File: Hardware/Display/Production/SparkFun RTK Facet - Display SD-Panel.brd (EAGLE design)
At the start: 118.6 x 193.8 mm, 662 parts, among them J1 FPC_12_0.5MM_BACKFLIP, J10 FPC_12_0.5MM_BACKFLIP, J11 FPC_12_0.5MM_BACKFLIP, J12 MICRO-SD-PUSH-PUSH-EXT-PIN, J13 FPC_12_0.5MM_BACKFLIP, J14 FPC_12_0.5MM_BACKFLIP, J15 MICRO-SD-PUSH-PUSH-EXT-PIN, J16 FPC_12_0.5MM_BACKFLIP, J17 FPC_12_0.5MM_BACKFLIP, J18 MICRO-SD-PUSH-PUSH-EXT-PIN, J19 FPC_12_0.5MM_BACKFLIP, J2 MICRO-SD-PUSH-PUSH-EXT-PIN, J20 FPC_12_0.5MM_BACKFLIP, J21 MICRO-SD-PUSH-PUSH-EXT-PIN, J22 FPC_12_0.5MM_BACKFLIP, J23 FPC_12_0.5MM_BACKFLIP, J24 MICRO-SD-PUSH-PUSH-EXT-PIN, J25 FPC_12_0.5MM_BACKFLIP, J26 FPC_12_0.5MM_BACKFLIP, J27 MICRO-SD-PUSH-PUSH-EXT-PIN, J28 FPC_12_0.5MM_BACKFLIP, J29 FPC_12_0.5MM_BACKFLIP, J3 FPC_12_0.5MM_BACKFLIP, J30 MICRO-SD-PUSH-PUSH-EXT-PIN, J31 FPC_12_0.5MM_BACKFLIP, J32 FPC_12_0.5MM_BACKFLIP, J33 MICRO-SD-PUSH-PUSH-EXT-PIN, J34 FPC_12_0.5MM_BACKFLIP, J35 FPC_12_0.5MM_BACKFLIP, J36 MICRO-SD-PUSH-PUSH-EXT-PIN, J37 FPC_12_0.5MM_BACKFLIP, J38 FPC_12_0.5MM_BACKFLIP, J39 MICRO-SD-PUSH-PUSH-EXT-PIN, J4 FPC_12_0.5MM_BACKFLIP, J40 FPC_12_0.5MM_BACKFLIP, J41 FPC_12_0.5MM_BACKFLIP, J42 MICRO-SD-PUSH-PUSH-EXT-PIN, J43 FPC_12_0.5MM_BACKFLIP, J44 FPC_12_0.5MM_BACKFLIP, J45 MICRO-SD-PUSH-PUSH-EXT-PIN, J46 FPC_12_0.5MM_BACKFLIP, J47 FPC_12_0.5MM_BACKFLIP, J48 MICRO-SD-PUSH-PUSH-EXT-PIN, J5 FPC_12_0.5MM_BACKFLIP, J6 MICRO-SD-PUSH-PUSH-EXT-PIN, J7 FPC_12_0.5MM_BACKFLIP, J8 FPC_12_0.5MM_BACKFLIP, J9 MICRO-SD-PUSH-PUSH-EXT-PIN, U1 LIS2DH12, U10 LIS2DH12, U11 LIS2DH12, U12 LIS2DH12, U13 LIS2DH12, U14 LIS2DH12, U15 LIS2DH12, U16 LIS2DH12, U2 LIS2DH12, U3 LIS2DH12, U4 LIS2DH12, U5 LIS2DH12, U6 LIS2DH12, U7 LIS2DH12, U8 LIS2DH12, U9 LIS2DH12

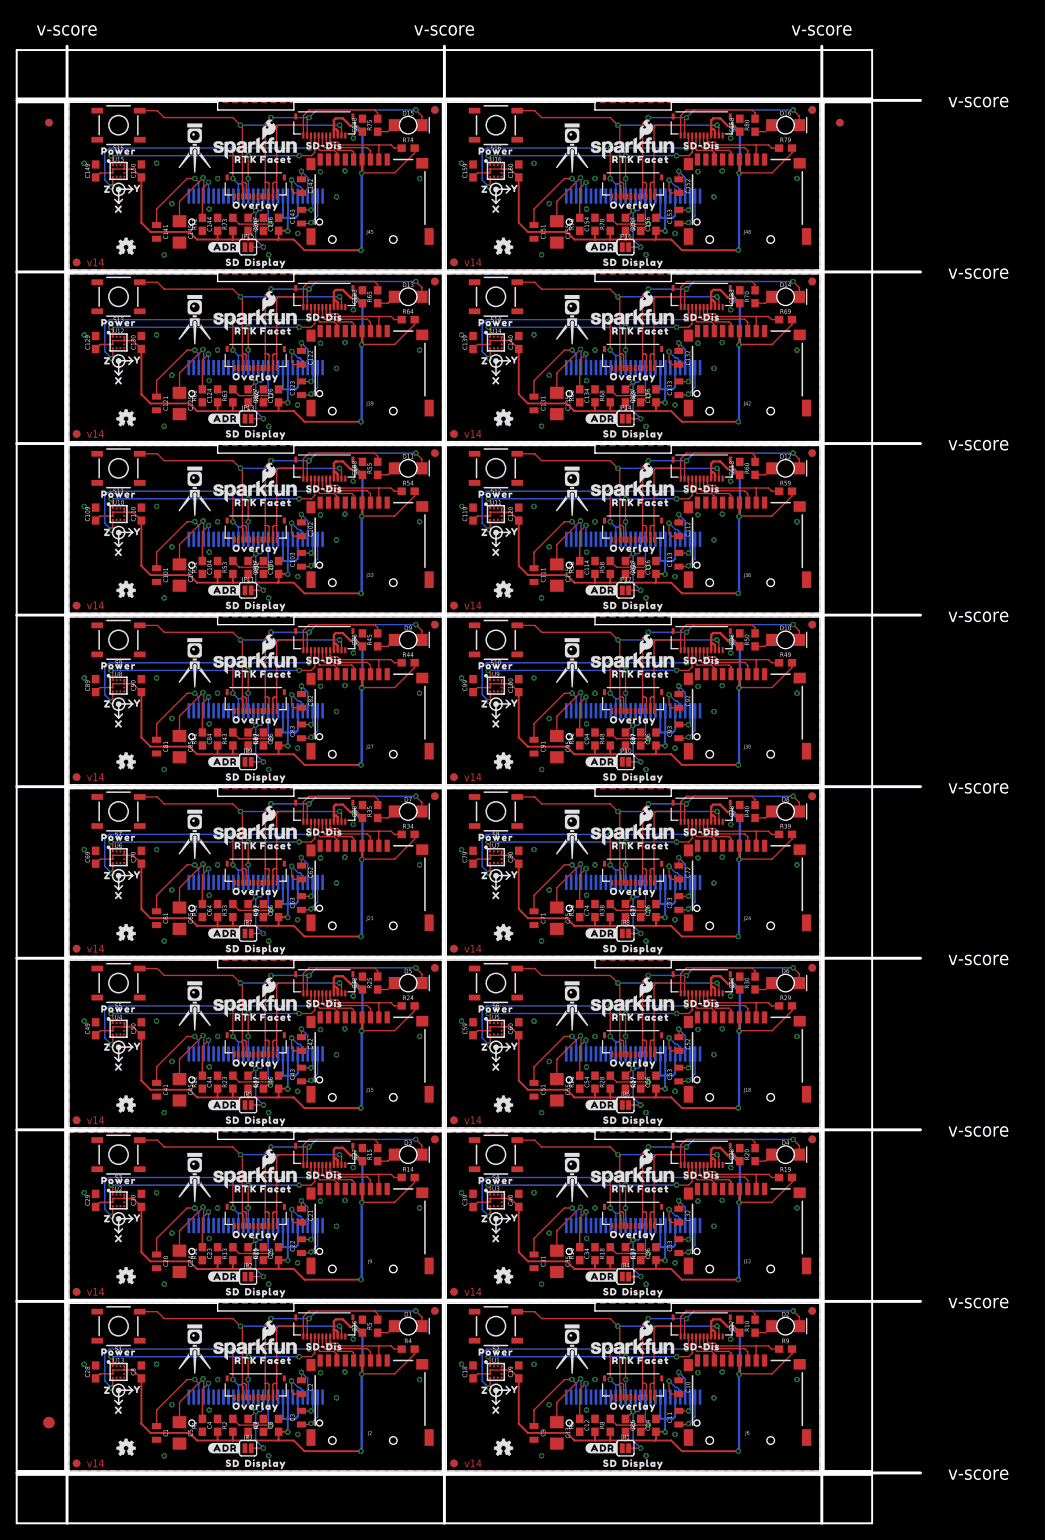
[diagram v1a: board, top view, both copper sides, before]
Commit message: Change to LIF 6 pin connector, remove GND plane around accel.
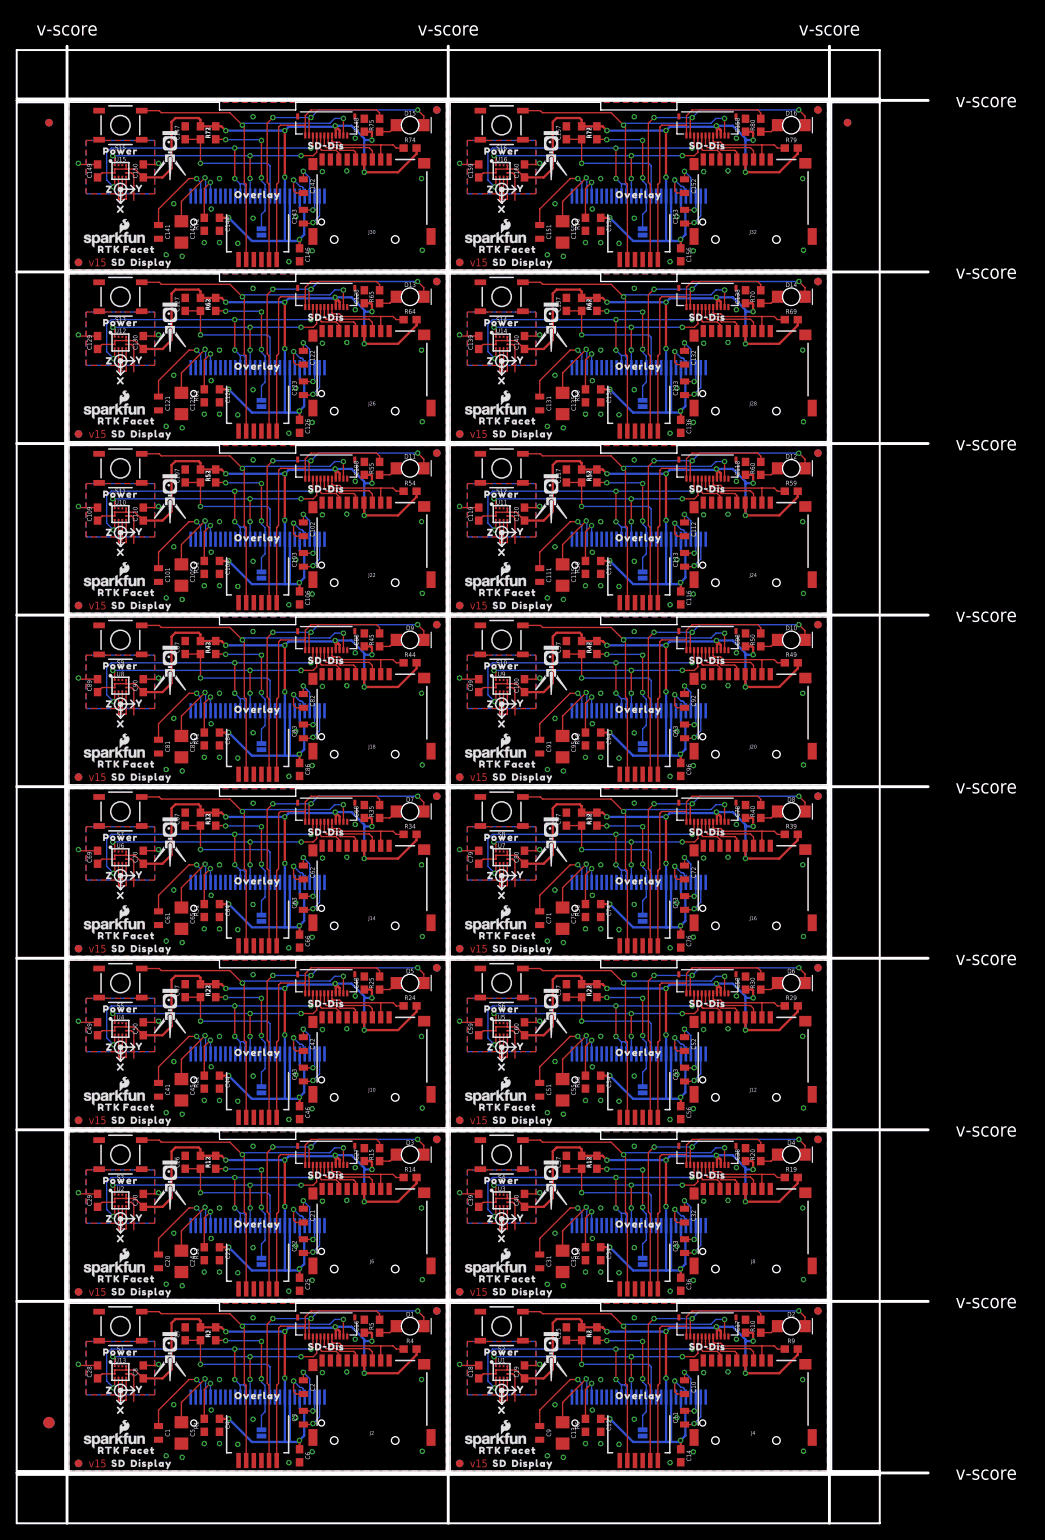
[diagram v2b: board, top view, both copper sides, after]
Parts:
- removed J33, J36, J39, J42, J45, J48: MICRO-SD-PUSH-PUSH-EXT-PIN, SparkFun-Connectors:MICROSD-EXTERNALPIN
- removed J34, J35, J37, J38, J40, J41, J43, J44, J46, J47: FPC_12_0.5MM_BACKFLIP, RTK Facet:FPC_12_DOUBLESIDED_BACKFLIP
- added JP17, JP19, JP21, JP23, JP25, JP27, JP29, JP31: (no value), SparkFun-Jumpers:SMT-JUMPER_2_NO_SILK
- added JP18, JP20, JP22, JP24, JP26, JP28, JP30, JP32: CONN_06, 1mm Pitch Connector:FPC_6_1MM-LIF
- J10, J14, J16, J20, J22, J26, J28, J32, J4, J8: value FPC_12_0.5MM_BACKFLIP -> MICRO-SD-PUSH-PUSH-EXT-PIN; device RTK Facet:FPC_12_DOUBLESIDED_BACKFLIP -> SparkFun-Connectors:MICROSD-EXTERNALPIN
- J15, J21, J27, J9: value MICRO-SD-PUSH-PUSH-EXT-PIN -> FPC_12_0.5MM_BACKFLIP; device SparkFun-Connectors:MICROSD-EXTERNALPIN -> RTK Facet:FPC_12_DOUBLESIDED_BACKFLIP
- JP1, JP10, JP12, JP14, JP16, JP4, JP6, JP8: value (none) -> CONN_06; device SparkFun-Jumpers:SMT-JUMPER_2_NO_SILK -> 1mm Pitch Connector:FPC_6_1MM-LIF
- LOGO10, LOGO12, LOGO14, LOGO16, LOGO18, LOGO2, LOGO20, LOGO22, LOGO24, LOGO26, LOGO28, LOGO30, LOGO32, LOGO5, LOGO6, LOGO8: value SFE_LOGO_NAME_FLAME.1_INCH -> SFE_LOGO_NAME_FLAME8_MM; device SparkFun-Aesthetics:SFE_LOGO_NAME_FLAME_.1 -> SparkFun-Aesthetics:SFE_LOGO_NAME_FLAME_8MM
- moved JP15 102.1 mm to (75.3, 72.5), flipped to the bottom, turned to 90 degrees
- moved JP16 88.7 mm to (74.8, 71.9), turned to 180 degrees
- moved J29 85.6 mm to (33.8, 176.6)
- moved J30 83.6 mm to (39.8, 161.6)
- moved JP11 83.5 mm to (75.3, 50.0), flipped to the bottom, turned to 90 degrees
- moved JP14 81.9 mm to (24.8, 71.9), turned to 180 degrees
- moved J32 75.5 mm to (89.8, 161.6), turned to 0 degrees
- moved J27 74.6 mm to (83.8, 154.0), turned to 180 degrees
- moved J31 67.5 mm to (83.8, 176.6)
- moved JP7 67.3 mm to (75.3, 27.5), flipped to the bottom, turned to 90 degrees
- moved J20 67.1 mm to (89.8, 94.0), turned to 0 degrees
- moved J18 66.7 mm to (39.8, 94.0)
- moved J17 66.6 mm to (33.8, 109.0)
- moved JP12 66.2 mm to (74.8, 49.4), turned to 180 degrees
- moved J8 65.6 mm to (89.8, 26.5), turned to 0 degrees
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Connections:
- net 3.3V1: now also J3.3, J3.4; no longer J4.3, J6.4
- net 3.3V10: now also J21.3, J21.4, J22.4; no longer J31.3, J31.4, J33.4
- net 3.3V11: now also J23.3, J23.4, J24.4; no longer J34.3, J34.4, J36.4
- net 3.3V12: now also J25.3, J25.4, J26.4; no longer J37.3, J37.4, J39.4
- net 3.3V13: now also J27.3, J27.4, J28.4; no longer J40.3, J40.4, J42.4
- net 3.3V14: now also J29.3, J29.4, J30.4; no longer J43.3, J43.4, J45.4
- net 3.3V15: now also J31.3, J31.4, J32.4; no longer J46.3, J46.4, J48.4
- net 3.3V2: now also J5.3, J5.4, J6.4; no longer J7.3, J7.4, J9.4
- net 3.3V3: now also J7.3, J7.4, J8.4; no longer J10.3, J10.4, J12.4
- net 3.3V4: now also J10.4, J9.3, J9.4; no longer J13.3, J13.4, J15.4
- net 3.3V5: now also J11.3, J11.4, J12.4; no longer J16.3, J16.4, J18.4
- net 3.3V6: now also J13.3, J13.4, J14.4; no longer J19.3, J19.4, J21.4
- net 3.3V7: now also J15.3, J15.4, J16.4; no longer J22.3, J22.4, J24.4
- net 3.3V8: now also J17.3, J17.4, J18.4; no longer J25.3, J25.4, J27.4
- net 3.3V9: now also J19.3, J19.4, J20.4; no longer J28.3, J28.4, J30.4
- net CHARGE_LED: now also JP1.2; no longer J3.3, J3.4
- net CHARGE_LED1: now also J3.11, JP4.2; no longer J4.11, J5.3, J5.4
- net CHARGE_LED10: now also J21.11, JP22.2; no longer J31.11, J32.3, J32.4
- net CHARGE_LED11: now also J23.11, JP24.2; no longer J34.11, J35.3, J35.4
- net CHARGE_LED12: now also J25.11, JP26.2; no longer J37.11, J38.3, J38.4
- net CHARGE_LED13: now also J27.11, JP28.2; no longer J40.11, J41.3, J41.4
- net CHARGE_LED14: now also J29.11, JP30.2; no longer J43.11, J44.3, J44.4
- net CHARGE_LED15: now also J31.11, JP32.2; no longer J46.11, J47.3, J47.4
- net CHARGE_LED2: now also J5.11, JP6.2; no longer J7.11, J8.3, J8.4
- net CHARGE_LED3: now also J7.11, JP8.2; no longer J10.11, J11.3, J11.4
- net CHARGE_LED4: now also J9.11, JP10.2; no longer J13.11, J14.3, J14.4
- net CHARGE_LED5: now also J11.11, JP12.2; no longer J16.11, J17.3, J17.4
- net CHARGE_LED6: now also J13.11, JP14.2; no longer J19.11, J20.3, J20.4
- net CHARGE_LED7: now also J15.11, JP16.2; no longer J22.11, J23.3, J23.4
- net CHARGE_LED8: now also J17.11, JP18.2; no longer J25.11, J26.3, J26.4
- net CHARGE_LED9: now also J19.11, JP20.2; no longer J28.11, J29.3, J29.4
- net D/C1: now also JP2.2; no longer JP1.2
- net D/C10: now also JP21.2; no longer JP11.2
- net D/C11: now also JP23.2; no longer JP12.2
- net D/C12: now also JP25.2; no longer JP13.2
- net D/C13: now also JP27.2; no longer JP14.2
- net D/C14: now also JP29.2; no longer JP15.2
- net D/C15: now also JP31.2; no longer JP16.2
- net D/C2: now also JP5.2; no longer JP2.2
- net D/C3: now also JP7.2; no longer JP4.2
- net D/C4: now also JP9.2; no longer JP5.2
- net D/C5: now also JP11.2; no longer JP6.2
- net D/C6: now also JP13.2; no longer JP7.2
- net D/C7: now also JP15.2; no longer JP8.2
- net D/C8: now also JP17.2; no longer JP9.2
- net D/C9: now also JP19.2; no longer JP10.2
- net ESP_21/SDA1: now also J3.10; no longer J4.10
- net ESP_21/SDA10: now also J21.10; no longer J31.10
- net ESP_21/SDA11: now also J23.10; no longer J34.10
- net ESP_21/SDA12: now also J25.10; no longer J37.10
- net ESP_21/SDA13: now also J27.10; no longer J40.10
- net ESP_21/SDA14: now also J29.10; no longer J43.10
- net ESP_21/SDA15: now also J31.10; no longer J46.10
- net ESP_21/SDA2: now also J5.10; no longer J7.10
- net ESP_21/SDA3: now also J7.10; no longer J10.10
- net ESP_21/SDA4: now also J9.10; no longer J13.10
- net ESP_21/SDA5: now also J11.10; no longer J16.10
- net ESP_21/SDA6: now also J13.10; no longer J19.10
- net ESP_21/SDA7: now also J15.10; no longer J22.10
- net ESP_21/SDA8: now also J17.10; no longer J25.10
- net ESP_21/SDA9: now also J19.10; no longer J28.10
- net ESP_22/SCL1: now also J3.9; no longer J4.9
- net ESP_22/SCL10: now also J21.9; no longer J31.9
- net ESP_22/SCL11: now also J23.9; no longer J34.9
- net ESP_22/SCL12: now also J25.9; no longer J37.9
- net ESP_22/SCL13: now also J27.9; no longer J40.9
- net ESP_22/SCL14: now also J29.9; no longer J43.9
- net ESP_22/SCL15: now also J31.9; no longer J46.9
- net ESP_22/SCL2: now also J5.9; no longer J7.9
- net ESP_22/SCL3: now also J7.9; no longer J10.9
- net ESP_22/SCL4: now also J9.9; no longer J13.9
- net ESP_22/SCL5: now also J11.9; no longer J16.9
- net ESP_22/SCL6: now also J13.9; no longer J19.9
- net ESP_22/SCL7: now also J15.9; no longer J22.9
- net ESP_22/SCL8: now also J17.9; no longer J25.9
- net ESP_22/SCL9: now also J19.9; no longer J28.9
- net GND: now also JP1.6; no longer J3.11, J3.12
- net GND1: now also J3.1, J4.10, J4.11, J4.12, J4.13, J4.6, J4.9, JP2.1, JP4.6; no longer J4.1, J5.11, J5.12, J6.10, J6.11, J6.12, J6.13, J6.6, J6.9, JP1.1
- net GND10: now also J21.1, J22.10, J22.11, J22.12, J22.13, J22.6, J22.9, JP21.1, JP22.6; no longer J31.1, J32.11, J32.12, J33.10, J33.11, J33.12, J33.13, J33.6, J33.9, JP11.1
- net GND11: now also J23.1, J24.10, J24.11, J24.12, J24.13, J24.6, J24.9, JP23.1, JP24.6; no longer J34.1, J35.11, J35.12, J36.10, J36.11, J36.12, J36.13, J36.6, J36.9, JP12.1
- net GND12: now also J25.1, J26.10, J26.11, J26.12, J26.13, J26.6, J26.9, JP25.1, JP26.6; no longer J37.1, J38.11, J38.12, J39.10, J39.11, J39.12, J39.13, J39.6, J39.9, JP13.1
- net GND13: now also J27.1, J28.10, J28.11, J28.12, J28.13, J28.6, J28.9, JP27.1, JP28.6; no longer J40.1, J41.11, J41.12, J42.10, J42.11, J42.12, J42.13, J42.6, J42.9, JP14.1
- net GND14: now also J29.1, J30.10, J30.11, J30.12, J30.13, J30.6, J30.9, JP29.1, JP30.6; no longer J43.1, J44.11, J44.12, J45.10, J45.11, J45.12, J45.13, J45.6, J45.9, JP15.1
- net GND15: now also J31.1, J32.10, J32.11, J32.12, J32.13, J32.6, J32.9, JP31.1, JP32.6; no longer J46.1, J47.11, J47.12, J48.10, J48.11, J48.12, J48.13, J48.6, J48.9, JP16.1
- net GND2: now also J5.1, J6.10, J6.11, J6.12, J6.13, J6.6, J6.9, JP5.1, JP6.6; no longer J7.1, J8.11, J8.12, J9.10, J9.11, J9.12, J9.13, J9.6, J9.9, JP2.1
- net GND3: now also J7.1, J8.10, J8.11, J8.12, J8.13, J8.6, J8.9, JP7.1, JP8.6; no longer J10.1, J11.11, J11.12, J12.10, J12.11, J12.12, J12.13, J12.6, J12.9, JP4.1
- net GND4: now also J10.10, J10.11, J10.12, J10.13, J10.6, J10.9, J9.1, JP10.6, JP9.1; no longer J13.1, J14.11, J14.12, J15.10, J15.11, J15.12, J15.13, J15.6, J15.9, JP5.1
- net GND5: now also J11.1, J12.10, J12.11, J12.12, J12.13, J12.6, J12.9, JP11.1, JP12.6; no longer J16.1, J17.11, J17.12, J18.10, J18.11, J18.12, J18.13, J18.6, J18.9, JP6.1
- net GND6: now also J13.1, J14.10, J14.11, J14.12, J14.13, J14.6, J14.9, JP13.1, JP14.6; no longer J19.1, J20.11, J20.12, J21.10, J21.11, J21.12, J21.13, J21.6, J21.9, JP7.1
- net GND7: now also J15.1, J16.10, J16.11, J16.12, J16.13, J16.6, J16.9, JP15.1, JP16.6; no longer J22.1, J23.11, J23.12, J24.10, J24.11, J24.12, J24.13, J24.6, J24.9, JP8.1
- net GND8: now also J17.1, J18.10, J18.11, J18.12, J18.13, J18.6, J18.9, JP17.1, JP18.6; no longer J25.1, J26.11, J26.12, J27.10, J27.11, J27.12, J27.13, J27.6, J27.9, JP9.1
- net GND9: now also J19.1, J20.10, J20.11, J20.12, J20.13, J20.6, J20.9, JP19.1, JP20.6; no longer J28.1, J29.11, J29.12, J30.10, J30.11, J30.12, J30.13, J30.6, J30.9, JP10.1
- net POWER_BTN: now also JP1.5; no longer J3.10, J3.9
- net POWER_BTN1: now also J3.2, JP4.5; no longer J4.2, J5.10, J5.9
- net POWER_BTN10: now also J21.2, JP22.5; no longer J31.2, J32.10, J32.9
- net POWER_BTN11: now also J23.2, JP24.5; no longer J34.2, J35.10, J35.9
- net POWER_BTN12: now also J25.2, JP26.5; no longer J37.2, J38.10, J38.9
- net POWER_BTN13: now also J27.2, JP28.5; no longer J40.2, J41.10, J41.9
- net POWER_BTN14: now also J29.2, JP30.5; no longer J43.2, J44.10, J44.9
- net POWER_BTN15: now also J31.2, JP32.5; no longer J46.2, J47.10, J47.9
- net POWER_BTN2: now also J5.2, JP6.5; no longer J7.2, J8.10, J8.9
- net POWER_BTN3: now also J7.2, JP8.5; no longer J10.2, J11.10, J11.9
- net POWER_BTN4: now also J9.2, JP10.5; no longer J13.2, J14.10, J14.9
- net POWER_BTN5: now also J11.2, JP12.5; no longer J16.2, J17.10, J17.9
- net POWER_BTN6: now also J13.2, JP14.5; no longer J19.2, J20.10, J20.9
- net POWER_BTN7: now also J15.2, JP16.5; no longer J22.2, J23.10, J23.9
- net POWER_BTN8: now also J17.2, JP18.5; no longer J25.2, J26.10, J26.9
- net POWER_BTN9: now also J19.2, JP20.5; no longer J28.2, J29.10, J29.9
- net SD_!CS!1: now also J3.5, J4.2; no longer J4.5, J6.2
- net SD_!CS!10: now also J21.5, J22.2; no longer J31.5, J33.2
- net SD_!CS!11: now also J23.5, J24.2; no longer J34.5, J36.2
- net SD_!CS!12: now also J25.5, J26.2; no longer J37.5, J39.2
- net SD_!CS!13: now also J27.5, J28.2; no longer J40.5, J42.2
- net SD_!CS!14: now also J29.5, J30.2; no longer J43.5, J45.2
- net SD_!CS!15: now also J31.5, J32.2; no longer J46.5, J48.2
- net SD_!CS!2: now also J5.5, J6.2; no longer J7.5, J9.2
- net SD_!CS!3: now also J7.5, J8.2; no longer J10.5, J12.2
- net SD_!CS!4: now also J10.2, J9.5; no longer J13.5, J15.2
- net SD_!CS!5: now also J11.5, J12.2; no longer J16.5, J18.2
- net SD_!CS!6: now also J13.5, J14.2; no longer J19.5, J21.2
- net SD_!CS!7: now also J15.5, J16.2; no longer J22.5, J24.2
- net SD_!CS!8: now also J17.5, J18.2; no longer J25.5, J27.2
- net SD_!CS!9: now also J19.5, J20.2; no longer J28.5, J30.2
- net SD_CIPO1: now also J3.8, J4.7; no longer J4.8, J6.7
- net SD_CIPO10: now also J21.8, J22.7; no longer J31.8, J33.7
- net SD_CIPO11: now also J23.8, J24.7; no longer J34.8, J36.7
- net SD_CIPO12: now also J25.8, J26.7; no longer J37.8, J39.7
- net SD_CIPO13: now also J27.8, J28.7; no longer J40.8, J42.7
- net SD_CIPO14: now also J29.8, J30.7; no longer J43.8, J45.7
- net SD_CIPO15: now also J31.8, J32.7; no longer J46.8, J48.7
- net SD_CIPO2: now also J5.8, J6.7; no longer J7.8, J9.7
- net SD_CIPO3: now also J7.8, J8.7; no longer J10.8, J12.7
- net SD_CIPO4: now also J10.7, J9.8; no longer J13.8, J15.7
- net SD_CIPO5: now also J11.8, J12.7; no longer J16.8, J18.7
- net SD_CIPO6: now also J13.8, J14.7; no longer J19.8, J21.7
- net SD_CIPO7: now also J15.8, J16.7; no longer J22.8, J24.7
- net SD_CIPO8: now also J17.8, J18.7; no longer J25.8, J27.7
- net SD_CIPO9: now also J19.8, J20.7; no longer J28.8, J30.7
- net SD_COPI1: now also J3.6, J4.3; no longer J4.6, J6.3
- net SD_COPI10: now also J21.6, J22.3; no longer J31.6, J33.3
- net SD_COPI11: now also J23.6, J24.3; no longer J34.6, J36.3
- net SD_COPI12: now also J25.6, J26.3; no longer J37.6, J39.3
- net SD_COPI13: now also J27.6, J28.3; no longer J40.6, J42.3
- net SD_COPI14: now also J29.6, J30.3; no longer J43.6, J45.3
- net SD_COPI15: now also J31.6, J32.3; no longer J46.6, J48.3
- net SD_COPI2: now also J5.6, J6.3; no longer J7.6, J9.3
- net SD_COPI3: now also J7.6, J8.3; no longer J10.6, J12.3
- net SD_COPI4: now also J10.3, J9.6; no longer J13.6, J15.3
- net SD_COPI5: now also J11.6, J12.3; no longer J16.6, J18.3
- net SD_COPI6: now also J13.6, J14.3; no longer J19.6, J21.3
- net SD_COPI7: now also J15.6, J16.3; no longer J22.6, J24.3
- net SD_COPI8: now also J17.6, J18.3; no longer J25.6, J27.3
- net SD_COPI9: now also J19.6, J20.3; no longer J28.6, J30.3
- net SD_SCK1: now also J3.7, J4.5; no longer J4.7, J6.5
- net SD_SCK10: now also J21.7, J22.5; no longer J31.7, J33.5
- net SD_SCK11: now also J23.7, J24.5; no longer J34.7, J36.5
- net SD_SCK12: now also J25.7, J26.5; no longer J37.7, J39.5
- net SD_SCK13: now also J27.7, J28.5; no longer J40.7, J42.5
- net SD_SCK14: now also J29.7, J30.5; no longer J43.7, J45.5
- net SD_SCK15: now also J31.7, J32.5; no longer J46.7, J48.5
- net SD_SCK2: now also J5.7, J6.5; no longer J7.7, J9.5
- net SD_SCK3: now also J7.7, J8.5; no longer J10.7, J12.5
- net SD_SCK4: now also J10.5, J9.7; no longer J13.7, J15.5
- net SD_SCK5: now also J11.7, J12.5; no longer J16.7, J18.5
- net SD_SCK6: now also J13.7, J14.5; no longer J19.7, J21.5
- net SD_SCK7: now also J15.7, J16.5; no longer J22.7, J24.5
- net SD_SCK8: now also J17.7, J18.5; no longer J25.7, J27.5
- net SD_SCK9: now also J19.7, J20.5; no longer J28.7, J30.5
- net V_USB: now also JP1.1; no longer J3.1, J3.2
- net V_USB1: now also J3.12, JP4.1; no longer J4.12, J5.1, J5.2
- net V_USB10: now also J21.12, JP22.1; no longer J31.12, J32.1, J32.2
- net V_USB11: now also J23.12, JP24.1; no longer J34.12, J35.1, J35.2
- net V_USB12: now also J25.12, JP26.1; no longer J37.12, J38.1, J38.2
- net V_USB13: now also J27.12, JP28.1; no longer J40.12, J41.1, J41.2
- net V_USB14: now also J29.12, JP30.1; no longer J43.12, J44.1, J44.2
- net V_USB15: now also J31.12, JP32.1; no longer J46.12, J47.1, J47.2
- net V_USB2: now also J5.12, JP6.1; no longer J7.12, J8.1, J8.2
- net V_USB3: now also J7.12, JP8.1; no longer J10.12, J11.1, J11.2
- net V_USB4: now also J9.12, JP10.1; no longer J13.12, J14.1, J14.2
- net V_USB5: now also J11.12, JP12.1; no longer J16.12, J17.1, J17.2
- net V_USB6: now also J13.12, JP14.1; no longer J19.12, J20.1, J20.2
- net V_USB7: now also J15.12, JP16.1; no longer J22.12, J23.1, J23.2
- net V_USB8: now also J17.12, JP18.1; no longer J25.12, J26.1, J26.2
- net V_USB9: now also J19.12, JP20.1; no longer J28.12, J29.1, J29.2
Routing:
- net GND8: track 0.00 -> 19.4 mm, vias 13 -> 20
- net GND10: track 0.00 -> 19.4 mm, vias 13 -> 20
- net GND9: track 0.00 -> 19.4 mm, vias 13 -> 20
- net GND11: track 0.00 -> 19.4 mm, vias 13 -> 20
- net GND4: track 0.00 -> 19.4 mm, vias 13 -> 20
- net GND2: track 0.00 -> 19.4 mm, vias 13 -> 20
- net GND: track 0.00 -> 19.4 mm, vias 13 -> 20
- net GND5: track 0.00 -> 19.4 mm, vias 13 -> 20
- net GND1: track 0.00 -> 19.4 mm, vias 13 -> 20
- net GND3: track 0.00 -> 19.4 mm, vias 13 -> 20
- net GND7: track 0.00 -> 19.4 mm, vias 13 -> 20
- net GND6: track 0.00 -> 19.4 mm, vias 13 -> 20
- net GND12: track 0.00 -> 19.4 mm, vias 13 -> 20
- net GND13: track 0.00 -> 19.4 mm, vias 13 -> 20
- net GND14: track 0.00 -> 19.4 mm, vias 13 -> 20
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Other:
- board size 118.6 x 193.8 mm -> 119.6 x 193.8 mm
- board text added: "v15"
- board text removed: "v14"
